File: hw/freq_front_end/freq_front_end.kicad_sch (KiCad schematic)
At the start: 5 parts, among them U1 OPA310SxDBV, U2 74LVC1G17, U3 SN74LV161APWR, U4 HMC363, U5 BFP196

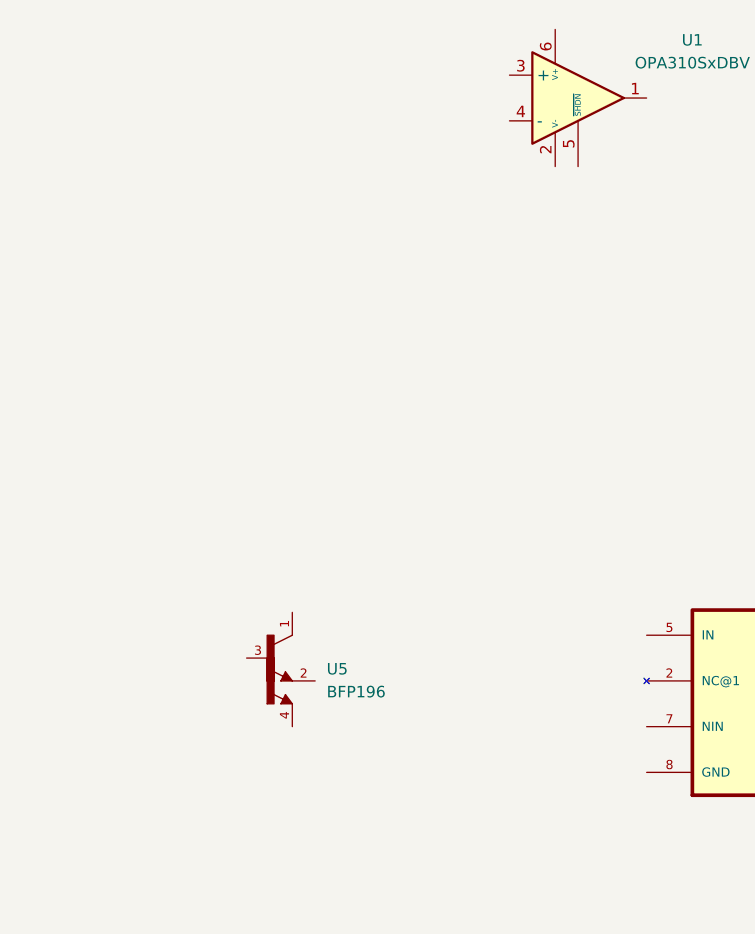
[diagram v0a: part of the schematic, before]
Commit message: 108 - add HMC433E
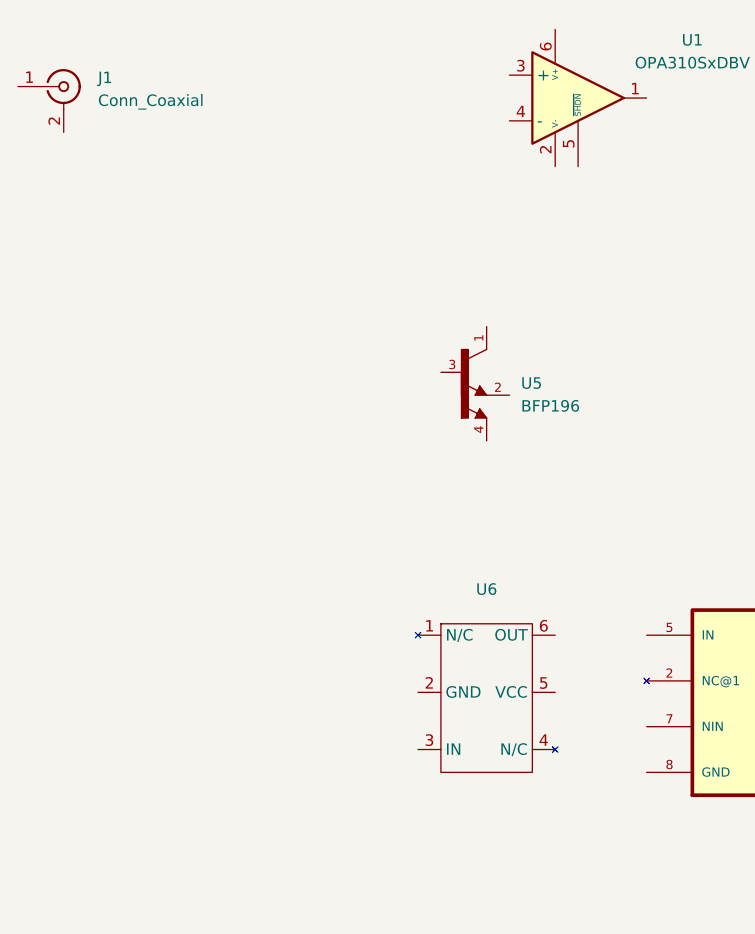
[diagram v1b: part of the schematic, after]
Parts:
- added J1: Conn_Coaxial, Connector_Coaxial:BNC_TEConnectivity_1478035_Horizontal, symbol Connector:Conn_Coaxial
- added U6: ~, HMC433E:SOT95P280X145-6N, symbol f4bjh_library:HMC433E
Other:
- moved on the sheet: U5
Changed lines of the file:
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@@
 	(symbol
 		(lib_id "BFP196:BFP196")
-		(at 81.28 99.06 0)
+		(at 102.87 67.31 0)
 		(unit 1)
 		(exclude_from_sim no)
@@
 		(fields_autoplaced yes)
 		(property "Reference" "U5"
-			(at 87.63 100.2918 0)
+			(at 109.22 68.5418 0)
 			(effects
 				(font
@@
 		)
 		(property "Value" "BFP196"
-			(at 87.63 102.8318 0)
+			(at 109.22 71.0818 0)
 			(effects
 				(font
@@
 		)
 		(property "Footprint" "BFP196:SOT143"
-			(at 81.28 99.06 0)
+			(at 102.87 67.31 0)
 			(effects
 				(font
@@
 		)
 		(property "Datasheet" ""
-			(at 81.28 99.06 0)
+			(at 102.87 67.31 0)
 			(effects
 				(font
@@
 		)
 		(property "Description" ""
-			(at 81.28 99.06 0)
+			(at 102.87 67.31 0)
 			(effects
 				(font
@@
 		)
 		(property "MF" "Infineon Technologies"
-			(at 81.28 99.06 0)
+			(at 102.87 67.31 0)
 			(effects
 				(font
@@
 		)
 		(property "Description_1" "RF Transistor NPN 12V 150mA 7.5GHz 700mW Surface Mount PG-SOT343-4"
-			(at 81.28 99.06 0)
+			(at 102.87 67.31 0)
 			(effects
 				(font
@@
 		)
 		(property "Package" "TO-253-4 Infineon Technologies"
-			(at 81.28 99.06 0)
+			(at 102.87 67.31 0)
 			(effects
 				(font
@@
 		)
 		(property "Price" "None"
-			(at 81.28 99.06 0)
+			(at 102.87 67.31 0)
 			(effects
 				(font
@@
 		)
 		(property "SnapEDA_Link" "https://www.snapeda.com/parts/BFP196/Infineon/view-part/?ref=snap"
-			(at 81.28 99.06 0)
+			(at 102.87 67.31 0)
 			(effects
 				(font
@@
 		)
 		(property "MP" "BFP196"
-			(at 81.28 99.06 0)
+			(at 102.87 67.31 0)
 			(effects
 				(font
@@
 		)
 		(property "Availability" "Not in stock"
-			(at 81.28 99.06 0)
+			(at 102.87 67.31 0)
 			(effects
 				(font
@@
 		)
 		(property "Check_prices" "https://www.snapeda.com/parts/BFP196/Infineon/view-part/?ref=eda"
-			(at 81.28 99.06 0)
+			(at 102.87 67.31 0)
 			(effects
 				(font
@@
 					(unit 1)
 				)
+			)
+		)
+	)
+	(symbol
+		(lib_id "Connector:Conn_Coaxial")
+		(at 58.42 35.56 0)
+		(unit 1)
+		(exclude_from_sim no)
+		(in_bom yes)
+		(on_board yes)
+		(dnp no)
+		(fields_autoplaced yes)
+		(property "Reference" "J1"
+			(at 62.23 34.5831 0)
+			(effects
+				(font
+					(size 1.27 1.27)
+				)
+				(justify left)
+			)
+		)
+		(property "Value" "Conn_Coaxial"
+			(at 62.23 37.1231 0)
+			(effects
+				(font
+					(size 1.27 1.27)
+				)
+				(justify left)
+			)
+		)
+		(property "Footprint" "Connector_Coaxial:BNC_TEConnectivity_1478035_Horizontal"
+			(at 58.42 35.56 0)
+			(effects
+				(font
+					(size 1.27 1.27)
+				)
+				(hide yes)
+			)
+		)
+		(property "Datasheet" "~"
+			(at 58.42 35.56 0)
+			(effects
+				(font
+					(size 1.27 1.27)
+				)
+				(hide yes)
+			)
+		)
+		(property "Description" "coaxial connector (BNC, SMA, SMB, SMC, Cinch/RCA, LEMO, ...)"
+			(at 58.42 35.56 0)
+			(effects
+				(font
+					(size 1.27 1.27)
+				)
+				(hide yes)
+			)
+		)
+		(pin "2"
+		)
+		(pin "1"
+		)
+		(instances
+			(project ""
+				(path "/111c022a-3320-492c-a4da-0a250f390ba3"
+					(reference "J1")
+					(unit 1)
+				)
+			)
+		)
+	)
+	(symbol
+		(lib_id "f4bjh_library:HMC433E")
+		(at 104.14 102.87 0)
+		(unit 1)
+		(exclude_from_sim no)
+		(in_bom yes)
+		(on_board yes)
+		(dnp no)
+		(fields_autoplaced yes)
+		(property "Reference" "U6"
+			(at 105.41 91.44 0)
+			(effects
+				(font
+					(size 1.27 1.27)
+				)
+			)
+		)
+		(property "Value" "~"
+			(at 105.41 93.98 0)
+			(effects
+				(font
+					(size 1.27 1.27)
+				)
+			)
+		)
+		(property "Footprint" "HMC433E:SOT95P280X145-6N"
+			(at 104.14 102.87 0)
+			(effects
+				(font
+					(size 1.27 1.27)
+				)
+				(hide yes)
+			)
+		)
+		(property "Datasheet" ""
+			(at 104.14 102.87 0)
+			(effects
+				(font
+					(size 1.27 1.27)
+				)
+				(hide yes)
+			)
+		)
+		(property "Description" ""
+			(at 104.14 102.87 0)
+			(effects
+				(font
+					(size 1.27 1.27)
+				)
+				(hide yes)
+			)
+		)
+		(pin "3"
+		)
+		(pin "2"
+		)
+		(pin "4"
+		)
+		(pin "6"
+		)
+		(pin "1"
+		)
+		(pin "5"
+		)
+		(instances
+			(project ""
+				(path "/111c022a-3320-492c-a4da-0a250f390ba3"
+					(reference "U6")
+					(unit 1)
+				)

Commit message: 108 - schematic wip
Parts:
- added C1, C2: C, Capacitor_SMD:C_1206_3216Metric, symbol Device:C
- added C10, C11, C12, C13, C14, C4, C5, C6, C7, C8, C9: C, symbol Device:C
- added C3: C_Polarized, symbol Device:C_Polarized
- added D1: LL4148, Diode_SMD:D_MiniMELF, symbol Diode:LL4148
- added D2: D_Zener, symbol Device:D_Zener
- added D3: BAT60A, Diode_SMD:D_SOD-323, symbol Diode:BAT60A
- added IC1: ERA-2+, ERA2, symbol f4bjh_library:ERA-2+
- added J2, J3: Conn_Coaxial, symbol Connector:Conn_Coaxial
- added J4: Conn_01x09_Socket, symbol Connector:Conn_01x09_Socket
- added J5: Conn_01x02_Socket, symbol Connector:Conn_01x02_Socket
- added L1, L2, L3: L, symbol Device:L
- added R1, R2, R3, R4, R7: R, Resistor_SMD:R_1206_3216Metric, symbol Device:R
- added R5, R6: R, symbol Device:R
- U6: value ~ -> HMC433E
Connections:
- net at U4.5 (IN): now also C7.2
- net at U4.7 (NIN): now also C8.2
- net GND: now reaches U4.8 (GND)
- net GND: now also U5.2, U5.4, C14.1, C3.2, C4.2, C5.2, C8.1, D1.2 (A), D2.2 (A), IC1.2 (GND_1), IC1.4 (GND_2), J2.2 (Ext), J3.2 (Ext), J4.9 (Pin_9), J5.2 (Pin_2), R4.2, R5.2
- net at U5.1: now also C2.1, C6.1, R1.2, R2.2
- net at U5.3: now also D1.1 (K), R2.1, R3.2
- new net: L1.1, R1.1
- new net: C3.1, C4.1, D2.1 (K), L1.2, L2.1
- new net: C5.1, D3.1 (K), R5.1, R6.1
- new net: C7.1, IC1.3 (RF-OUT_AND_DC-IN), L3.2
- new net: C2.2, D3.2 (A), R4.1
- new net: L3.1, R7.1
- new net: C14.2, R7.2
- new net: C1.2, R3.1
- new net: C13.2, IC1.1 (RF_IN)
- new net: C1.1, J2.1 (In)
- new net: C13.1, J3.1 (In)
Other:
- moved on the sheet: J1, U1, U2, U3, U4, U5, U6
